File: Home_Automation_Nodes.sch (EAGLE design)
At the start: 19 parts

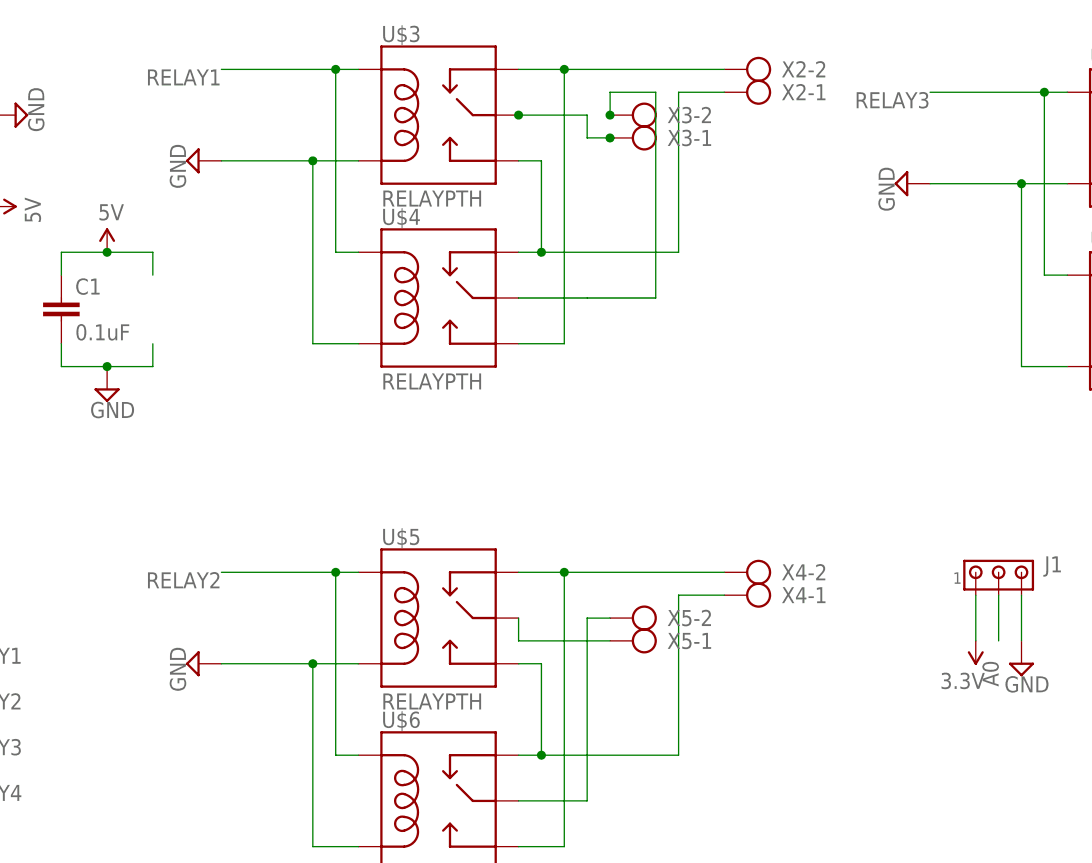
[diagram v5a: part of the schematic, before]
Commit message: ULN connection fix. Changed coil connection from GND to 5V
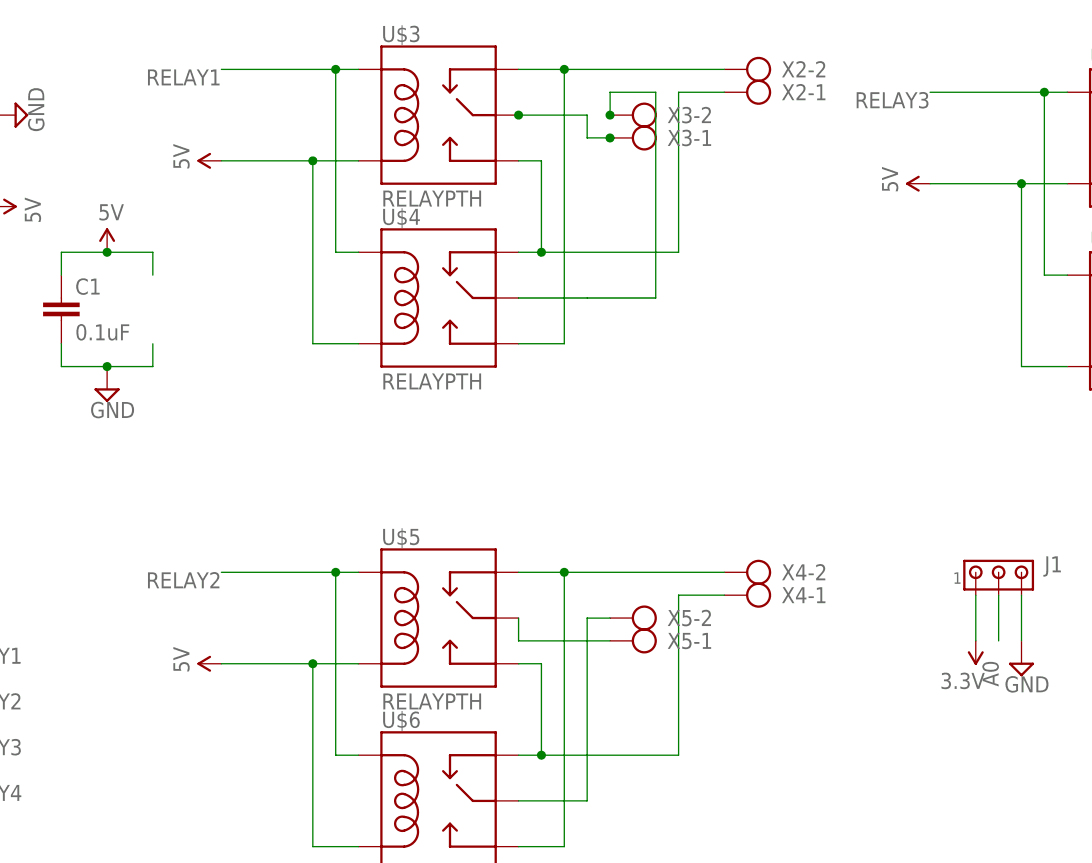
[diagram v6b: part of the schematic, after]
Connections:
- net 5V: now also U$3.COIL0, U$4.COIL0, U$5.COIL0, U$6.COIL0, U$7.COIL0, U$8.COIL0
- net GND: no longer U$3.COIL0, U$4.COIL0, U$5.COIL0, U$6.COIL0, U$7.COIL0, U$8.COIL0
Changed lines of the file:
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@@
 <?xml version="1.0" encoding="utf-8"?>
 <!DOCTYPE eagle SYSTEM "eagle.dtd">
-<eagle version="7.3.0">
+<eagle version="7.6.0">
 <drawing>
 <settings>
@@
 <part name="SUPPLY8" library="SparkFun-Aesthetics" deviceset="5V" device=""/>
 <part name="SUPPLY9" library="supply2" deviceset="GND" device=""/>
-<part name="SUPPLY10" library="supply2" deviceset="GND" device=""/>
-<part name="SUPPLY11" library="supply2" deviceset="GND" device=""/>
-<part name="SUPPLY12" library="supply2" deviceset="GND" device=""/>
 <part name="J1" library="con-amp" deviceset="MTA03-100" device=""/>
 <part name="J2" library="con-amp" deviceset="MTA07-100" device=""/>
@@
 <part name="SUPPLY17" library="supply2" deviceset="GND" device=""/>
 <part name="SUPPLY14" library="supply2" deviceset="GND" device=""/>
+<part name="SUPPLY10" library="SparkFun-Aesthetics" deviceset="5V" device=""/>
+<part name="SUPPLY11" library="SparkFun-Aesthetics" deviceset="5V" device=""/>
+<part name="SUPPLY12" library="SparkFun-Aesthetics" deviceset="5V" device=""/>
 </parts>
 <sheets>
@@
 <instance part="SUPPLY8" gate="G$1" x="-10.16" y="27.94" rot="R270"/>
 <instance part="SUPPLY9" gate="GND" x="-48.26" y="27.94" rot="R270"/>
-<instance part="SUPPLY10" gate="GND" x="20.32" y="68.58" rot="R270"/>
-<instance part="SUPPLY11" gate="GND" x="20.32" y="124.46" rot="R270"/>
-<instance part="SUPPLY12" gate="GND" x="99.06" y="121.92" rot="R270"/>
 <instance part="J1" gate="G$1" x="109.22" y="78.74"/>
 <instance part="J2" gate="G$1" x="132.08" y="78.74"/>
@@
 <instance part="SUPPLY17" gate="GND" x="10.16" y="99.06"/>
 <instance part="SUPPLY14" gate="GND" x="111.76" y="68.58"/>
+<instance part="SUPPLY10" gate="G$1" x="22.86" y="124.46" rot="R90"/>
+<instance part="SUPPLY11" gate="G$1" x="22.86" y="68.58" rot="R90"/>
+<instance part="SUPPLY12" gate="G$1" x="101.6" y="121.92" rot="R90"/>
 </instances>
 <busses>
@@
 <junction x="10.16" y="114.3"/>
 </segment>
-</net>
-<net name="GND" class="0">
-<segment>
-<pinref part="U$1" gate="G$1" pin="GND"/>
-<wire x1="-7.62" y1="86.36" x2="-10.16" y2="86.36" width="0.1524" layer="91"/>
-<pinref part="SUPPLY7" gate="GND" pin="GND"/>
-</segment>
-<segment>
-<pinref part="SUPPLY9" gate="GND" pin="GND"/>
-<pinref part="ULN1" gate="G$1" pin="9"/>
-<wire x1="-45.72" y1="27.94" x2="-40.64" y2="27.94" width="0.1524" layer="91"/>
+<segment>
+<pinref part="U$3" gate="G$1" pin="COIL0"/>
+<wire x1="38.1" y1="124.46" x2="33.02" y2="124.46" width="0.1524" layer="91"/>
+<pinref part="U$4" gate="G$1" pin="COIL0"/>
+<wire x1="33.02" y1="124.46" x2="22.86" y2="124.46" width="0.1524" layer="91"/>
+<wire x1="38.1" y1="104.14" x2="33.02" y2="104.14" width="0.1524" layer="91"/>
+<wire x1="33.02" y1="104.14" x2="33.02" y2="124.46" width="0.1524" layer="91"/>
+<junction x="33.02" y="124.46"/>
+<pinref part="SUPPLY10" gate="G$1" pin="5V"/>
 </segment>
 <segment>
@@
 <wire x1="33.02" y1="48.26" x2="33.02" y2="68.58" width="0.1524" layer="91"/>
 <junction x="33.02" y="68.58"/>
-<pinref part="SUPPLY10" gate="GND" pin="GND"/>
-</segment>
-<segment>
-<pinref part="U$3" gate="G$1" pin="COIL0"/>
-<wire x1="38.1" y1="124.46" x2="33.02" y2="124.46" width="0.1524" layer="91"/>
-<pinref part="U$4" gate="G$1" pin="COIL0"/>
-<wire x1="33.02" y1="124.46" x2="22.86" y2="124.46" width="0.1524" layer="91"/>
-<wire x1="38.1" y1="104.14" x2="33.02" y2="104.14" width="0.1524" layer="91"/>
-<wire x1="33.02" y1="104.14" x2="33.02" y2="124.46" width="0.1524" layer="91"/>
-<junction x="33.02" y="124.46"/>
-<pinref part="SUPPLY11" gate="GND" pin="GND"/>
+<pinref part="SUPPLY11" gate="G$1" pin="5V"/>
 </segment>
 <segment>
@@
 <wire x1="111.76" y1="101.6" x2="111.76" y2="121.92" width="0.1524" layer="91"/>
 <junction x="111.76" y="121.92"/>
-<pinref part="SUPPLY12" gate="GND" pin="GND"/>
-</segment>
-<segment>
+<pinref part="SUPPLY12" gate="G$1" pin="5V"/>
+</segment>
+</net>
+<net name="GND" class="0">
+<segment>
+<pinref part="U$1" gate="G$1" pin="GND"/>
+<wire x1="-7.62" y1="86.36" x2="-10.16" y2="86.36" width="0.1524" layer="91"/>
+<pinref part="SUPPLY7" gate="GND" pin="GND"/>
+</segment>
+<segment>
+<pinref part="SUPPLY9" gate="GND" pin="GND"/>
+<pinref part="ULN1" gate="G$1" pin="9"/>
+<wire x1="-45.72" y1="27.94" x2="-40.64" y2="27.94" width="0.1524" layer="91"/>
+</segment>
+<segment>
